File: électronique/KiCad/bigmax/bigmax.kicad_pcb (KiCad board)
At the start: 2 copper layers, 99.1 x 99.1 mm, 19 parts, among them SW1 SW_Push, U1 qtr-1rc_a, U10 batt_connector, U2 qtr-1rc_b, U3 dc_geared_encoder, U4 dc_geared_encoder, U5 TPS61090_dc_boost, U6 MT3608, U7 VL53L0X_a, U8 VL53L0X_b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

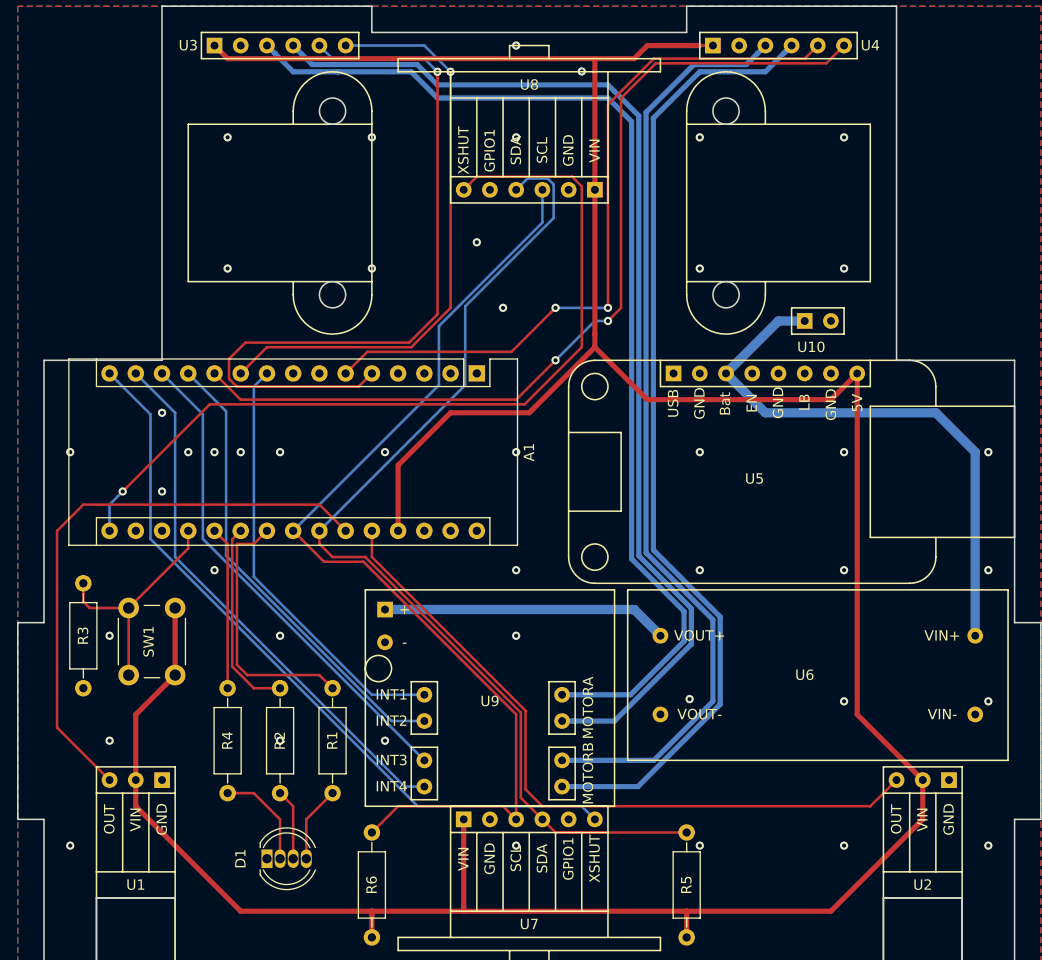
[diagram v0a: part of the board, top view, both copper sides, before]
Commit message: mise à jour du projet kicad en ajoutant des résistances de pull-up sur la commande des moteurs et une capacité de découplage en entrée du controller moteurs
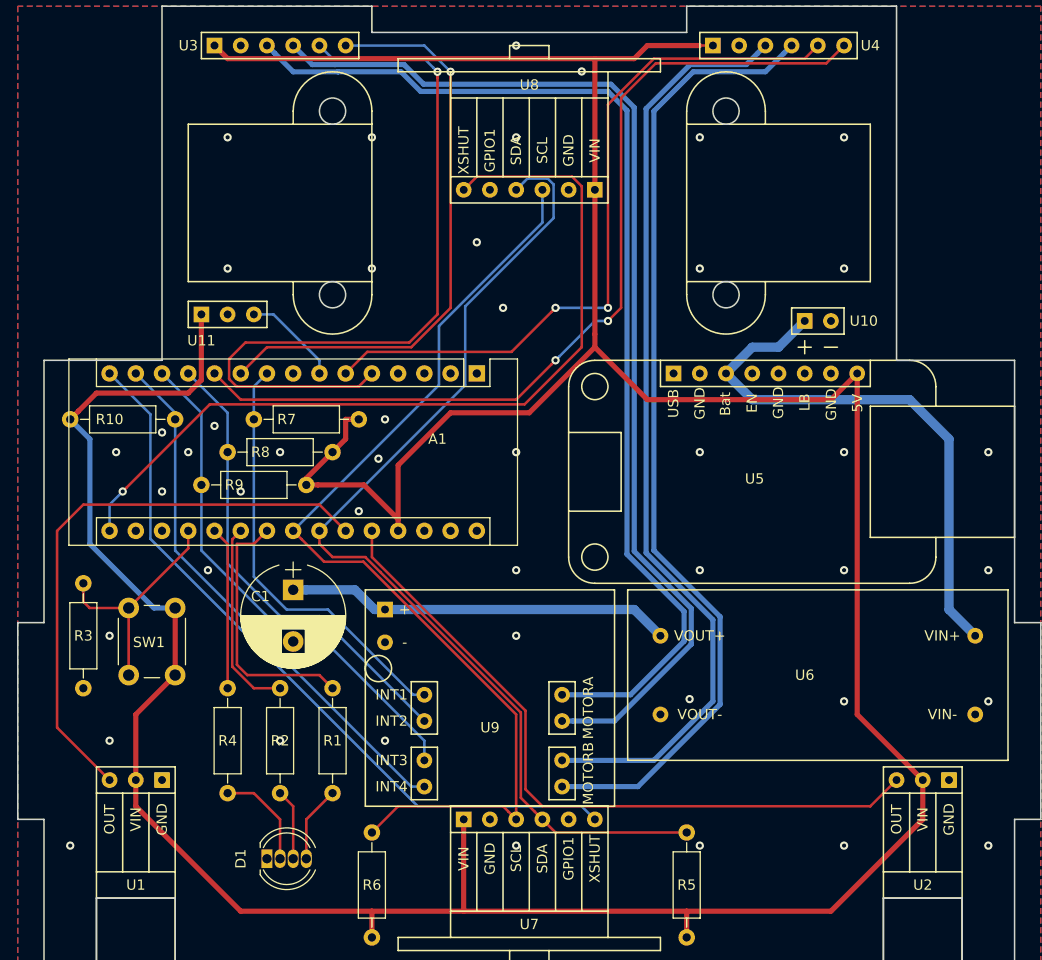
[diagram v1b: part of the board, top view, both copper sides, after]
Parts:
- added C1: 470µF, Capacitors_THT:CP_Radial_D10.0mm_P5.00mm, F.Cu at (127.0, 107.3)
- added R10: 4.7k, Resistors_THT:R_Axial_DIN0207_L6.3mm_D2.5mm_P10.16mm_Horizontal, F.Cu at (115.6, 90.8)
- added R7: 4.7k, Resistors_THT:R_Axial_DIN0207_L6.3mm_D2.5mm_P10.16mm_Horizontal, F.Cu at (123.2, 90.8)
- added R8: 4.7k, Resistors_THT:R_Axial_DIN0207_L6.3mm_D2.5mm_P10.16mm_Horizontal, F.Cu at (120.7, 94.0)
- added R9: 4.7k, Resistors_THT:R_Axial_DIN0207_L6.3mm_D2.5mm_P10.16mm_Horizontal, F.Cu at (118.1, 97.2)
- added U11: micro_start, bigmax:micro_start, F.Cu at (118.1, 80.6)
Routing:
- net VCC: track 300.6 -> 365.5 mm
- net +6V: track 27.7 -> 37.4 mm
- net Net-(A1-Pad7): track 0.00 -> 9.46 mm
- net /in3: track 48.0 -> 49.8 mm
- net +BATT: track 54.8 -> 54.0 mm
- net GND: vias 50 -> 51

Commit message: Dernière mise à jour du pcb BigMax v1 avant commande ajout des pins pour MicroStart
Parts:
- moved U11 0.63 mm to (118.1, 80.0)
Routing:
- net VCC: track 365.5 -> 360.2 mm
- net Net-(A1-Pad7): track 9.46 -> 11.2 mm
- net /XSHUT_b: track 82.5 -> 81.0 mm
- net /sda: track 97.7 -> 99.2 mm
- net /c2_b: track 88.1 -> 87.6 mm
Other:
- outline, holes or cut-outs redrawn

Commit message: Bigmax v2 - mai 2019
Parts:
- added J1: Conn_01x03, Pin_Headers:Pin_Header_Angled_1x03_Pitch2.54mm, F.Cu at (85.7, 112.4)
- added J2: Conn_01x02, Pin_Headers:Pin_Header_Angled_1x02_Pitch2.54mm, F.Cu at (127.0, 87.6)
- added J3: Conn_01x03_input, Pin_Headers:Pin_Header_Angled_1x03_Pitch2.54mm, B.Cu at (160.0, 113.7)
- added J4: Conn_01x02, Pin_Headers:Pin_Header_Angled_1x02_Pitch2.54mm, B.Cu at (226.1, 95.2)
- added U12: generic_bms_3s_10A, bigmax:generic_bms_3s_10A, B.Cu at (236.2, 102.9)
- added U13: generic_18650_3s_case, bigmax:CB-18650-PC6, F.Cu at (172.1, 48.9)
- D1: footprint LEDs:LED_D5.0mm-4 -> bigmax:LED_D5.0mm-4
- R3: value 1k -> 220
- R4: value 220 -> 1k
- U1: value qtr-1rc_a -> pololu_enc03b; footprint bigmax:qtr_1rc -> bigmax:pololu_enc03b
- U10: value batt_connector -> jsumo_micro_start; footprint bigmax:batt_connector -> bigmax:jsumo_micro_start
- U11: value micro_start -> generic_vertical_slide_switch; footprint bigmax:micro_start -> Pin_Headers:Pin_Header_Straight_1x03_Pitch2.54mm
- U2: value qtr-1rc_b -> pololu_enc03b; footprint bigmax:qtr_1rc -> bigmax:pololu_enc03b
- U3, U4: value dc_geared_encoder -> pololu_irs01a; footprint bigmax:dc_geared_encoder -> bigmax:pololu_irs01a
- U5: value TPS61090_dc_boost -> pololu_reg19a; footprint bigmax:dc_boost_500C -> bigmax:pololu_reg19a
- U6: value MT3608 -> pololu_reg04b; footprint bigmax:MT3608 -> bigmax:pololu_reg04b
- U7: value VL53L0X_a -> pololu_md17a; footprint bigmax:vl53l0x -> bigmax:pololu_md17a
- U8: value VL53L0X_b -> generic_vl53l0x; footprint bigmax:vl53l0x -> bigmax:generic_vl53l0x
- U9: value dc_driver_1A_3-14V -> generic_vl53l0x; footprint bigmax:MX1616 -> bigmax:generic_vl53l0x
- moved U11 117.2 mm to (234.9, 89.5)
- moved U8 98.3 mm to (69.8, 115.6), turned to 0 degrees
- moved U3 83.6 mm to (62.2, 115.6), turned to 180 degrees
- moved R5 80.8 mm to (85.7, 115.6)
- moved U2 78.6 mm to (127.0, 79.4)
- moved R4 74.1 mm to (52.1, 88.9)
- moved U4 69.9 mm to (133.3, 115.6), turned to 180 degrees
- moved R6 66.5 mm to (76.2, 99.1), turned to 90 degrees
- moved U7 64.2 mm to (93.3, 89.5), turned to 90 degrees
- moved U6 62.6 mm to (135.3, 87.6)
- moved SW1 61.7 mm to (54.0, 104.8)
- moved U1 60.0 mm to (76.2, 79.4)
- moved A1 57.2 mm to (87.6, 86.4)
- moved C1 47.2 mm to (88.9, 79.4), turned to 180 degrees
- moved R7 44.0 mm to (80.0, 99.1), turned to 90 degrees
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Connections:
- net Net-(A1-Pad21) renamed /led_green
- net Net-(A1-Pad22) renamed /led_blue
- A1 pad 1: Net-(A1-Pad1) -> (no net)
- A1 pad 17: Net-(A1-Pad17) -> (no net)
- A1 pad 18: Net-(A1-Pad18) -> (no net)
- A1 pad 2: Net-(A1-Pad2) -> (no net)
- A1 pad 20: Net-(A1-Pad20) -> /led_red
- A1 pad 27: VCC -> (no net)
- A1 pad 28: Net-(A1-Pad28) -> (no net)
- A1 pad 3: Net-(A1-Pad3) -> (no net)
- A1 pad 30: Net-(A1-Pad30) -> +12V
- A1 pad 8: Net-(A1-Pad8) -> (no net)
- D1 pad 1: GND -> Net-(D1-Pad1)
- D1 pad 2: Net-(D1-Pad2) -> GND
- R10 pad 1: /in4 -> +5V
- R10 pad 2: VCC -> /scl
- R3 pad 1: GND -> /led_red
- R3 pad 2: Net-(A1-Pad19) -> Net-(D1-Pad1)
- R4 pad 1: Net-(A1-Pad20) -> GND
- R4 pad 2: Net-(D1-Pad2) -> Net-(A1-Pad19)
- R5 pad 1: /scl -> +5V
- R5 pad 2: VCC -> /sda
- R6 pad 1: /sda -> /in3
- R6 pad 2: VCC -> +5V
- R7 pad 1: /in1 -> /in4
- R7 pad 2: VCC -> +5V
- R8 pad 2: VCC -> +5V
- R9 pad 1: /in3 -> /in1
- R9 pad 2: VCC -> +5V
- SW1 pad 1: VCC -> Net-(A1-Pad19)
- SW1 pad 2: Net-(A1-Pad19) -> +5V
- U1 pad 2: VCC -> /c2_a
- U1 pad 3: /out_a -> /c1_a
- U10 pad 1: +BATT -> Net-(J3-Pad3)
- U10 pad 2: GND -> Net-(J3-Pad1)
- U11 pad 1: VCC -> Net-(J4-Pad2)
- U11 pad 2: GND -> Net-(U11-Pad2)
- U11 pad 3: Net-(A1-Pad7) -> (no net)
- U2 pad 2: VCC -> /c2_b
- U2 pad 3: /out_b -> /c1_b
- U3 pad 1: VCC -> GND
- U3 pad 2: GND -> +5V
- U3 pad 3: /M1 -> /out_a
- U4 pad 1: VCC -> GND
- U4 pad 2: GND -> +5V
- U4 pad 3: /M3 -> /out_b
- U5 pad 1: Net-(U5-Pad1) -> (no net)
- U5 pad 2: GND -> (no net)
- U5 pad 3: +BATT -> +12V
- U5 pad 4: Net-(U5-Pad4) -> GND
- U5 pad 5: GND -> +6V
- U5 pad 6: Net-(U5-Pad6) -> GND
- U6 pad 1: +BATT -> +5V
- U6 pad 3: +6V -> +12V
- U6 pad 4: GND -> (no net)
- U7 pad 1: VCC -> GND
- U7 pad 2: GND -> (no net)
- U7 pad 3: /sda -> /in3
- U7 pad 4: /scl -> /in4
- U7 pad 5: Net-(U7-Pad5) -> /in2
- U7 pad 6: /XSHUT_a -> /in1
- U8 pad 1: VCC -> +5V
- U8 pad 3: /sda -> /scl
- U8 pad 4: /scl -> /sda
- U8 pad 5: Net-(U8-Pad5) -> (no net)
- U8 pad 6: /XSHUT_b -> /XSHUT_a
- U9 pad 1: +6V -> +5V
- U9 pad 3: /in1 -> /scl
- U9 pad 4: /in2 -> /sda
- U9 pad 5: /in3 -> (no net)
- U9 pad 6: /in4 -> /XSHUT_b
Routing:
- net VCC: track 360.2 -> 0.00 mm
- net +5V: track 0.00 -> 232.4 mm, vias 0 -> 2
- net /b2: track 0.00 -> 118.8 mm
- net /b1: track 0.00 -> 116.1 mm
- net /M4: track 94.7 -> 17.4 mm
- net /M3: track 91.1 -> 17.5 mm
- net /b+: track 0.00 -> 72.9 mm
- net +12V: track 0.00 -> 69.0 mm
- net /M2: track 105.4 -> 39.0 mm
- net /c1_a: track 74.3 -> 12.5 mm, vias 1 -> 0
- net /M1: track 105.1 -> 45.7 mm
- net +BATT: track 54.0 -> 0.00 mm
- net /led_red: track 0.00 -> 46.0 mm, vias 0 -> 2
- net /c2_a: track 57.4 -> 13.5 mm, vias 1 -> 0
- net /scl: track 100.5 -> 68.6 mm
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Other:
- board size 99.1 x 99.1 mm -> 190.5 x 94 mm
- board text added: "bigmax - v2.0.0 mai 2019"
- board text removed: "bigmax - v1.0.0 janvier 2019"
